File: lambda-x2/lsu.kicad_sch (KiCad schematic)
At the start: 56 parts, among them Q5 BSS169H6327, Q6 BSS169H6327, Q7 BSS169H6327, Q8 BSS169H6327, U12 MCP6002T-I/SN, U3 MCP6002T-I/SN, U9 GS8332-SR

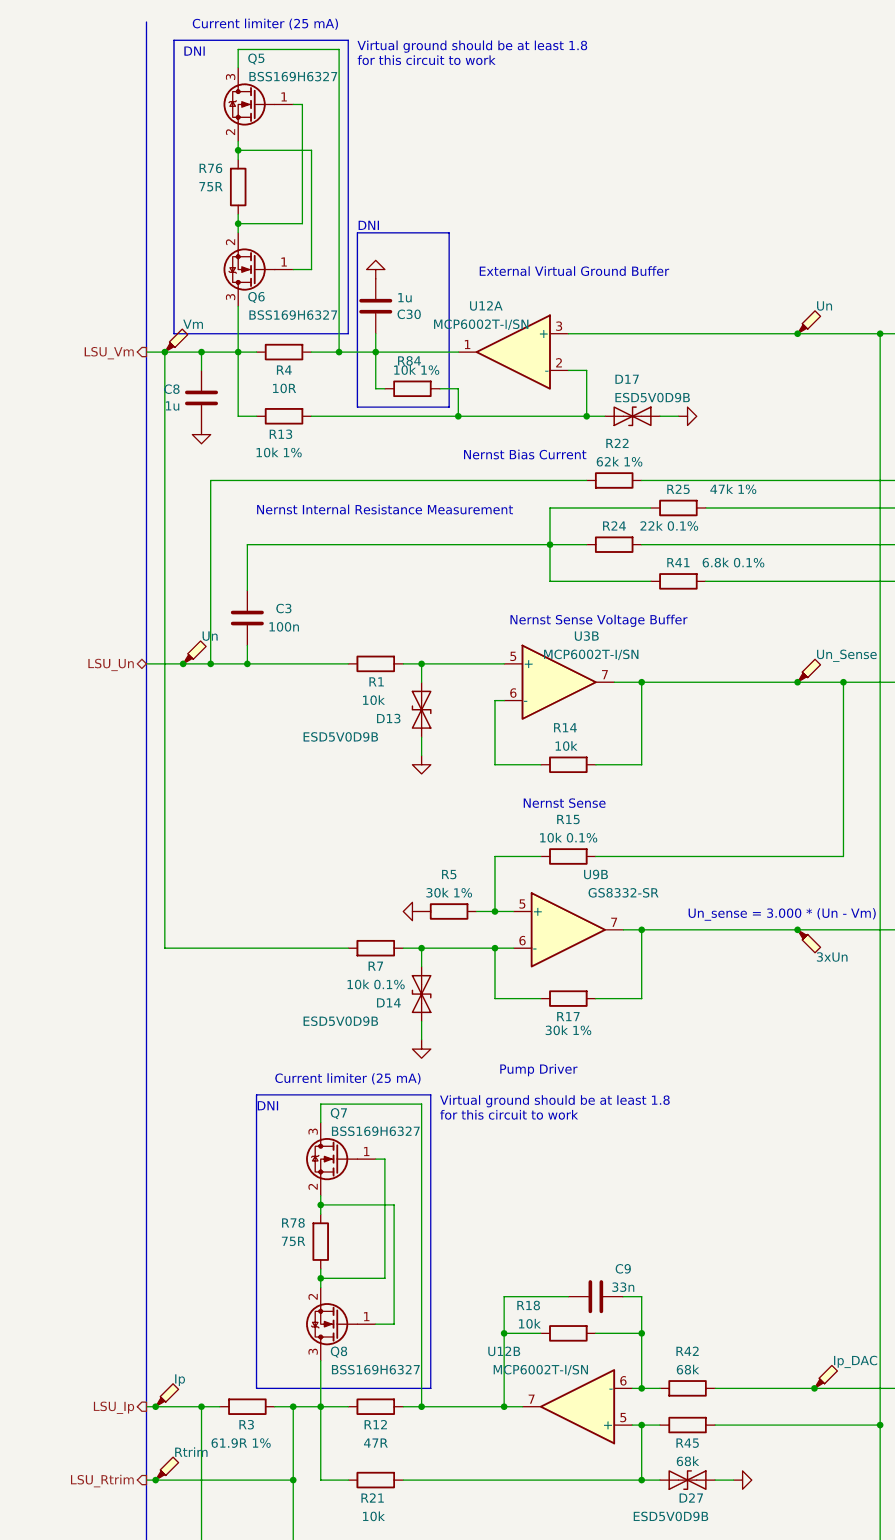
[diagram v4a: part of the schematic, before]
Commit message: lambda-x2: revork aux outputs, remove useless protection in LSU
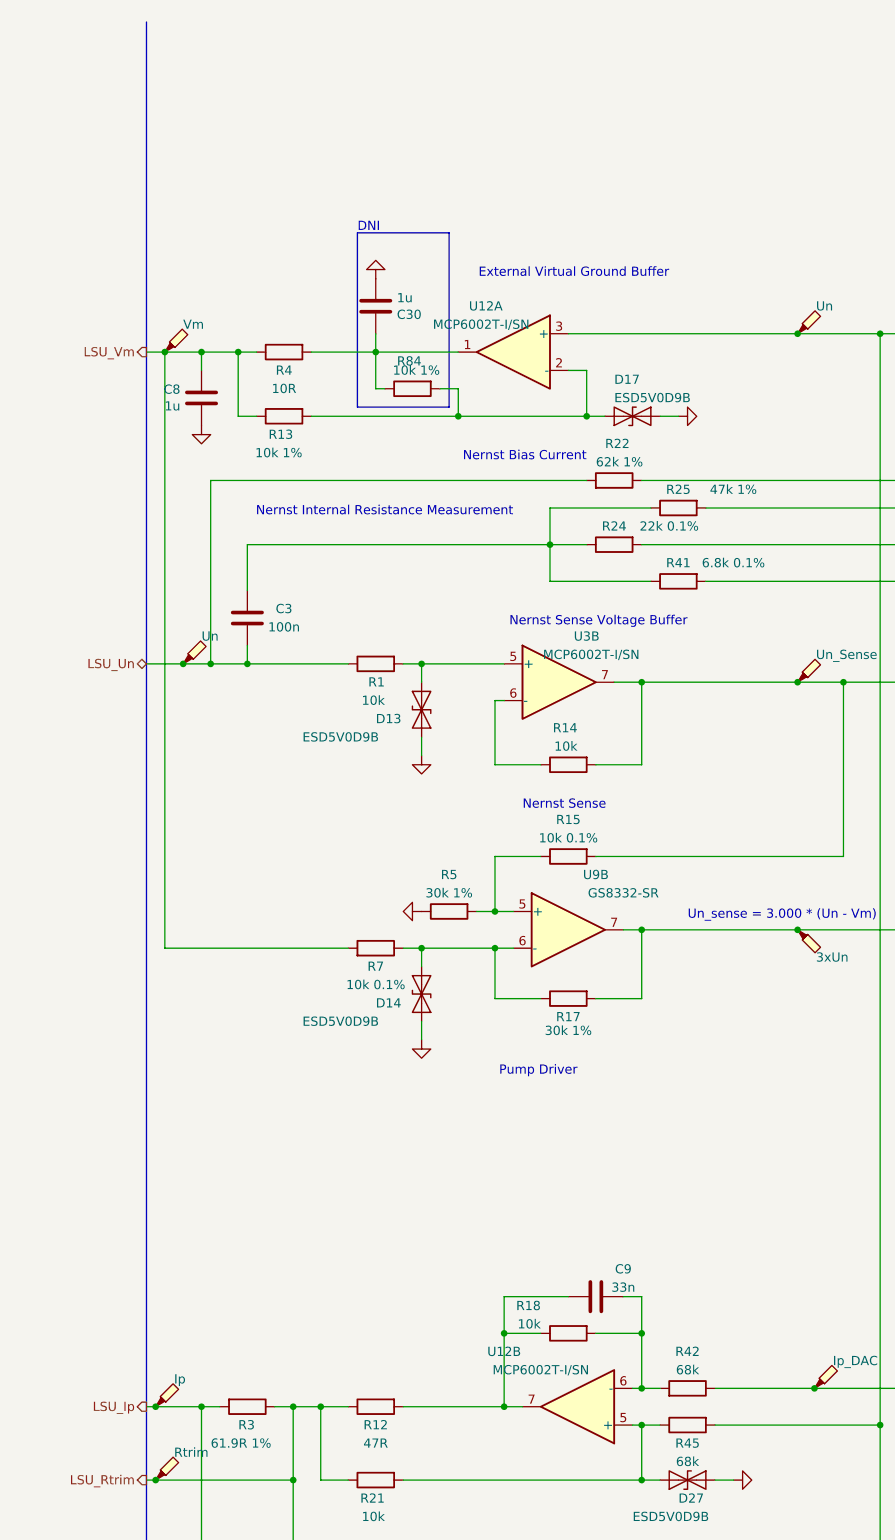
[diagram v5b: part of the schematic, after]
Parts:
- removed Q5, Q6, Q7, Q8: BSS169H6327, Package_TO_SOT_SMD:SOT-23, symbol Transistor_FET:BSS123
- removed R76, R78: 75R, Resistor_SMD:R_0603_1608Metric, symbol Device:R
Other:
- note removed: "Current limiter (25 mA)"
- note removed: "Virtual ground should be at least 1.8 for this circuit to work"

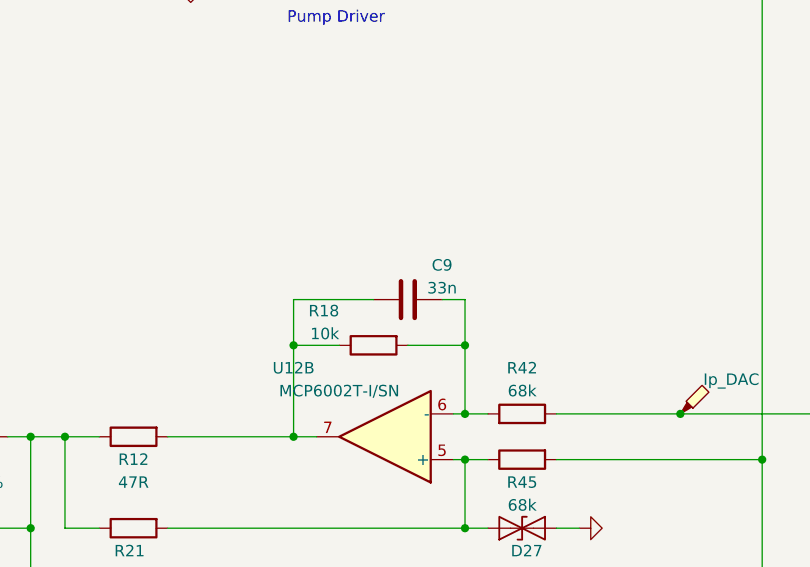
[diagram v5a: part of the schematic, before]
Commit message: lambda-x2: diagnostic for AUX out, PWM noise cancelation, etc
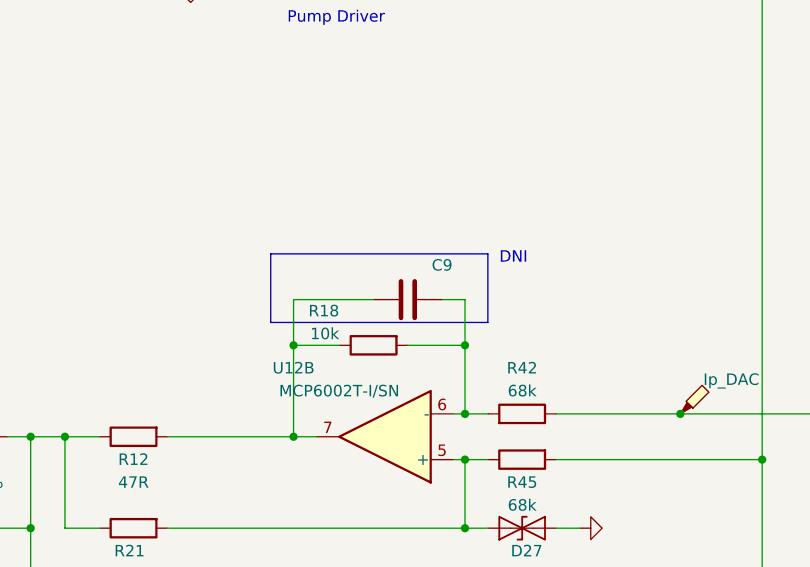
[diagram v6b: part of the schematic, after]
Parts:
- C9: value 33n -> (none); footprint Capacitor_SMD:C_0402_1005Metric -> (none); now left out of the parts list
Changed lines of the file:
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@@
+    (stroke (width 0) (type default) (color 0 0 0 0))
+  )
+  (polyline (pts (xy 151.13 204.47) (xy 151.13 196.85))
     (stroke (width 0) (type default) (color 0 0 0 0))
   )
@@
     (stroke (width 0) (type default) (color 0 0 0 0))
   )
+  (polyline (pts (xy 127 204.47) (xy 151.13 204.47))
+    (stroke (width 0) (type default) (color 0 0 0 0))
+  )
   (wire (pts (xy 227.33 167.64) (xy 227.33 162.56))
     (stroke (width 0) (type default) (color 0 0 0 0))
@@
     (stroke (width 0) (type default) (color 0 0 0 0))
   )
+  (polyline (pts (xy 127 196.85) (xy 127 204.47))
+    (stroke (width 0) (type default) (color 0 0 0 0))
+  )
   (wire (pts (xy 135.89 243.84) (xy 130.81 243.84))
     (stroke (width 0) (type default) (color 0 0 0 0))
@@
   )
   (wire (pts (xy 115.57 256.54) (xy 118.11 256.54))
+    (stroke (width 0) (type default) (color 0 0 0 0))
+  )
+  (polyline (pts (xy 151.13 196.85) (xy 127 196.85))
     (stroke (width 0) (type default) (color 0 0 0 0))
   )
@@
   (text "Nernst Internal Resistance Measurement" (at 130.81 93.98 180)
     (effects (font (size 1.27 1.27)) (justify right bottom))
+  )
+  (text "DNI" (at 152.4 198.12 0)
+    (effects (font (size 1.27 1.27)) (justify left bottom))
   )
   (text "caps for precision opamp" (at 210.82 237.49 0)
@@
   )
   (symbol (lib_id "Device:C") (at 142.24 201.93 90) (mirror x) (unit 1)
-    (in_bom yes) (on_board yes)
+    (in_bom no) (on_board yes)
     (property "Reference" "C9" (id 0) (at 146.05 198.12 90))
-    (property "Value" "33n" (id 1) (at 146.05 200.66 90))
-    (property "Footprint" "Capacitor_SMD:C_0402_1005Metric" (id 2) (at 146.05 202.8952 0)
-      (effects (font (size 1.27 1.27)) hide)
-    )
+    (property "Value" "" (id 1) (at 146.05 200.66 90))
+    (property "Footprint" "" (id 2) (at 146.05 202.8952 0)
+      (effects (font (size 1.27 1.27)) hide)
+    )

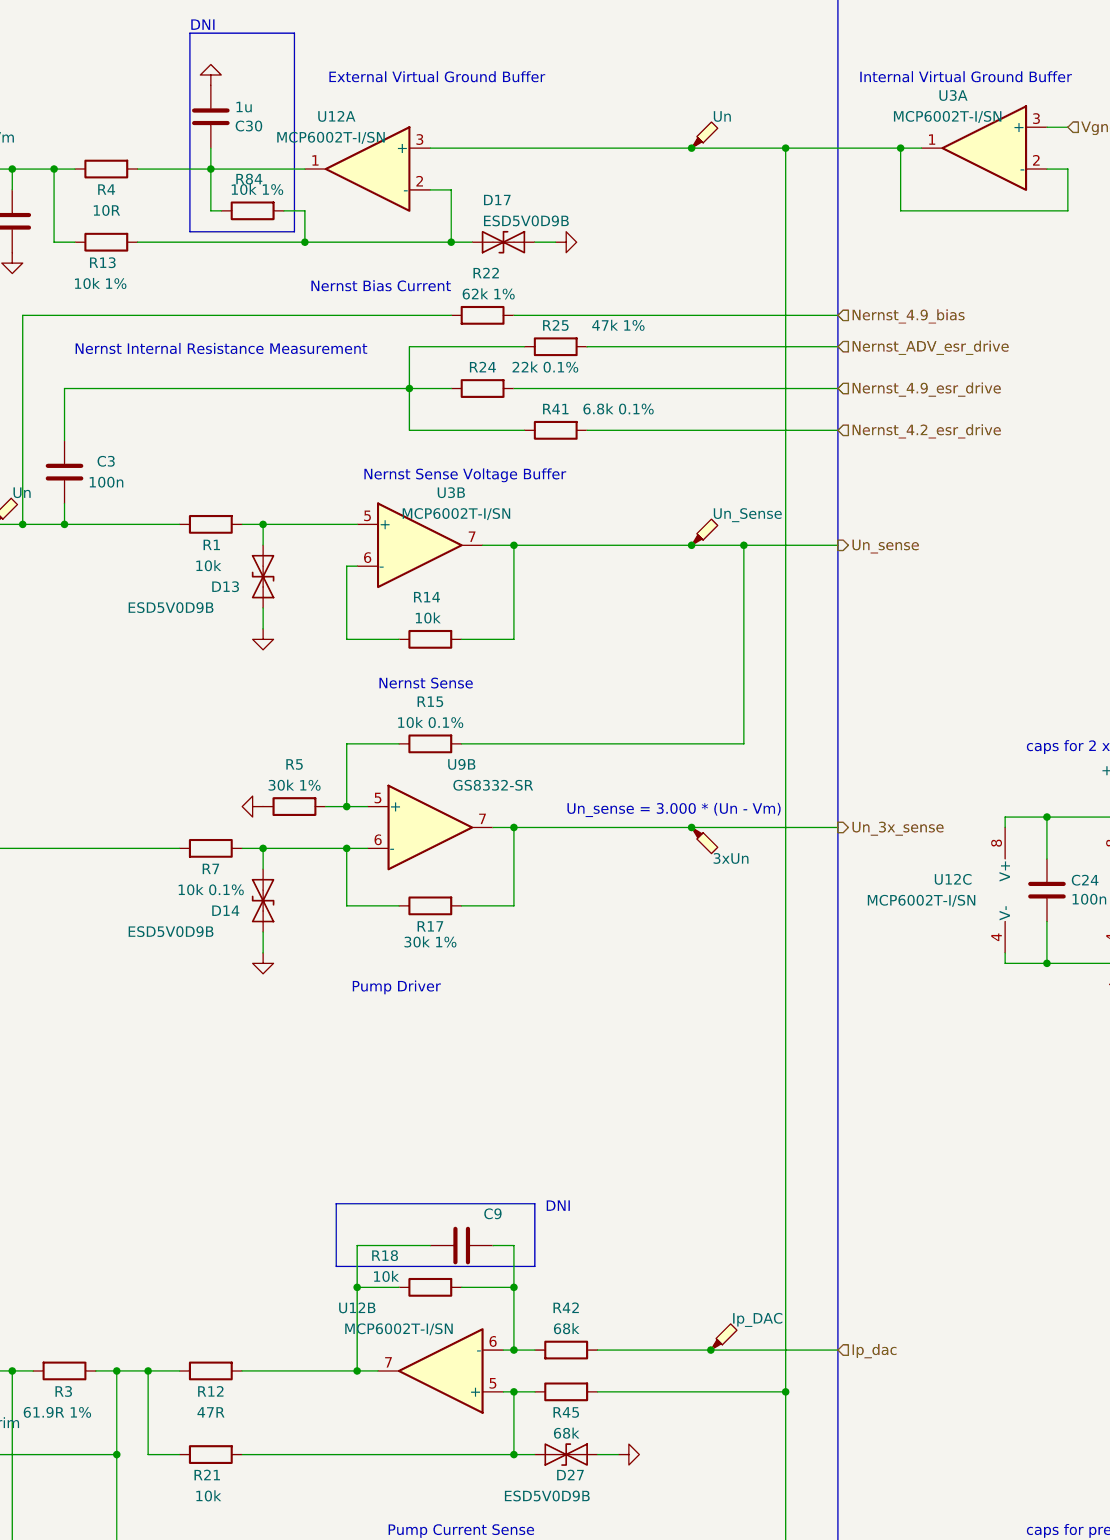
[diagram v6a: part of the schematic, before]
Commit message: lambda-x2: jtag, adc channels, one more led, BT en, etc
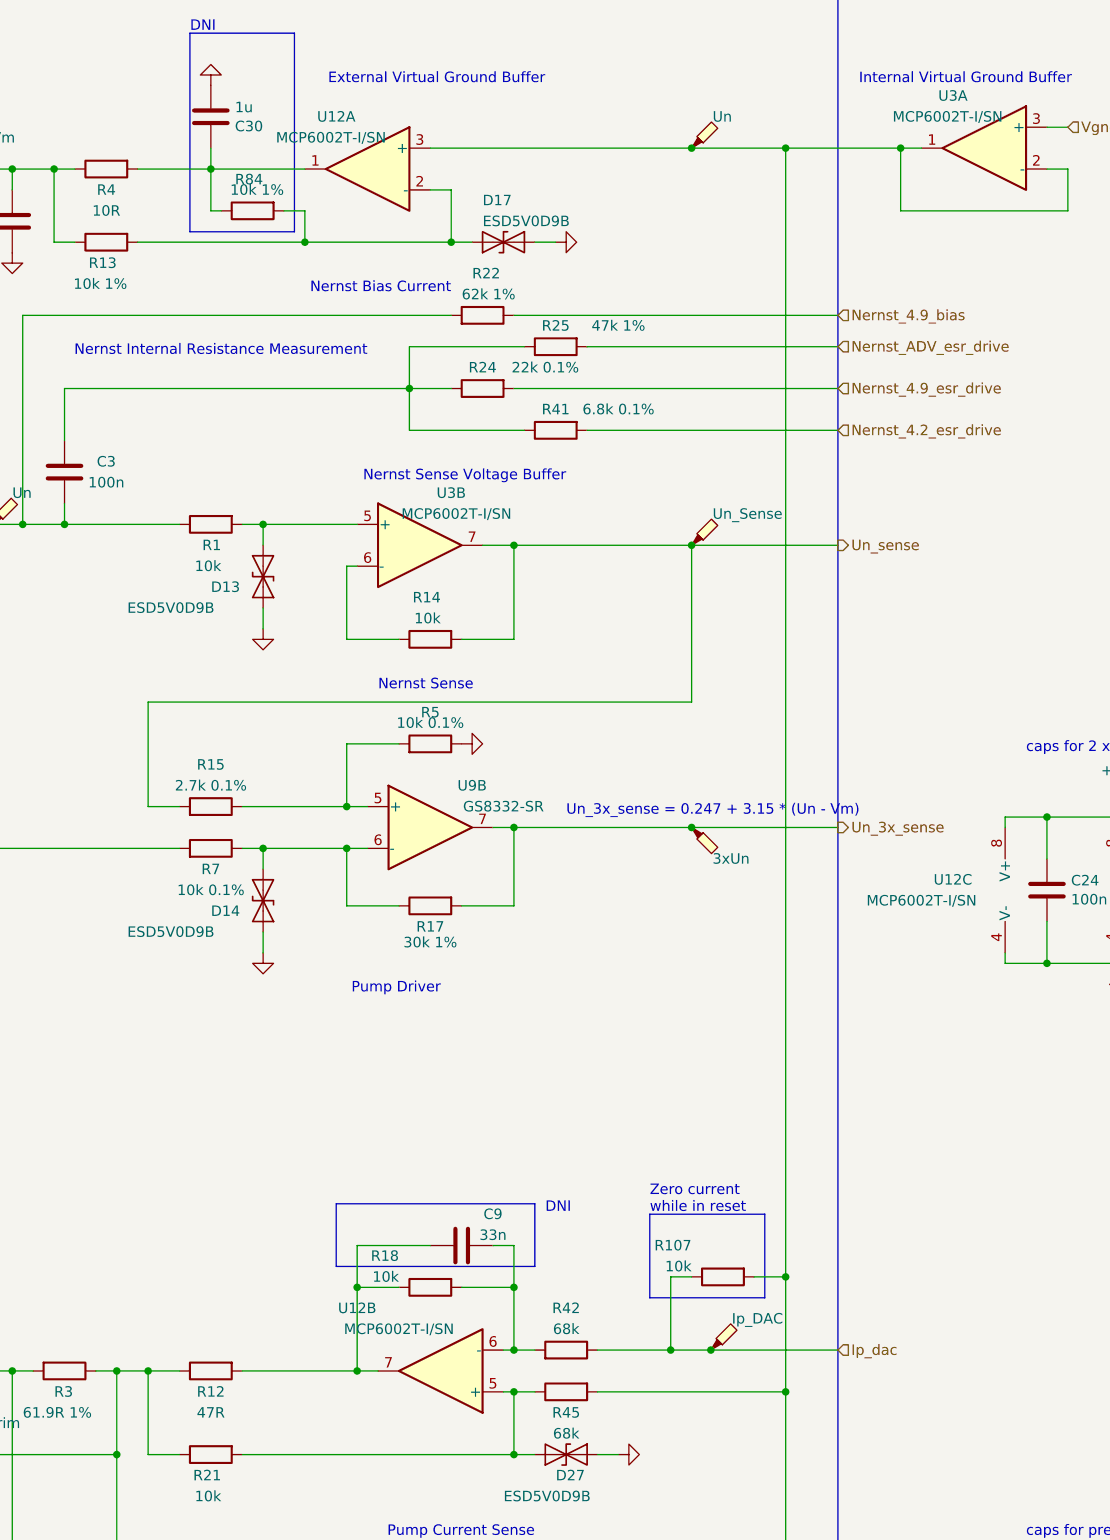
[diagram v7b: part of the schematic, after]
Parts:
- added R107: 10k, Resistor_SMD:R_0402_1005Metric, symbol Device:R
- C9: value (none) -> 33n; footprint (none) -> Capacitor_SMD:C_0402_1005Metric
- R15: value 10k 0.1% -> 2.7k 0.1%; LCSC C309083 -> C318131
- R5: value 30k 1% -> 10k 0.1%; LCSC C22984 -> C309083
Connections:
- net Ip_dac: now also R107.1
- net at R20.2, R45.2, TP14.1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: now also R107.2
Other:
- note added: "Un_3x_sense = 0.247 + 3.15 * (Un - Vm)"
- note added: "Zero current while in reset"
- note removed: "Un_sense = 3.000 * (Un - Vm)"
- moved on the sheet: R15, R5

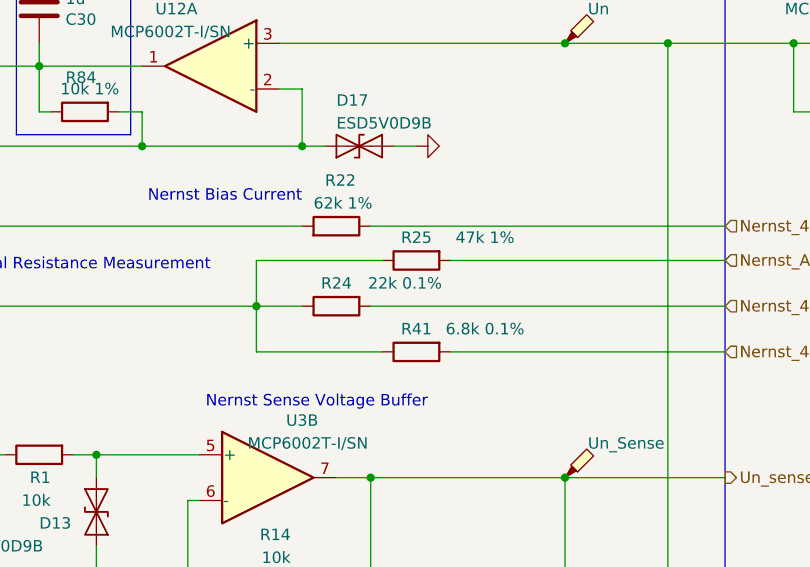
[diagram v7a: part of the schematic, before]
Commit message: lambda-x2: update BOM per JLC availability
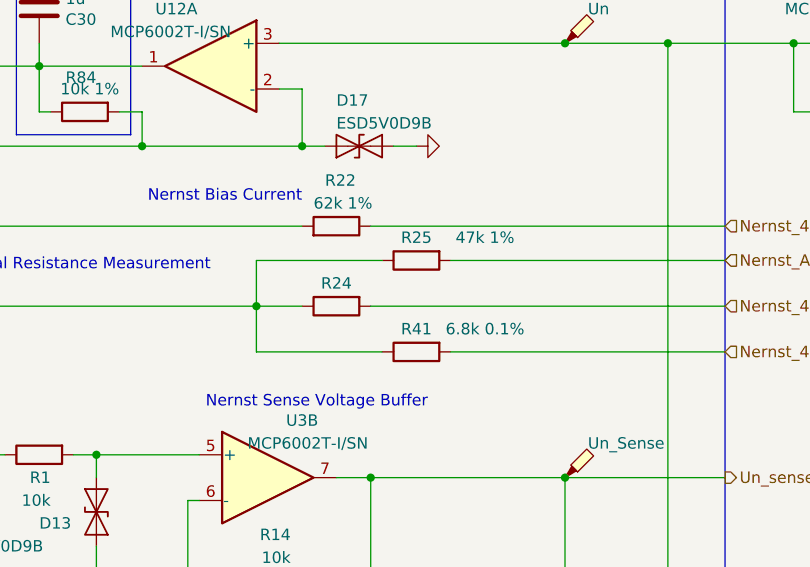
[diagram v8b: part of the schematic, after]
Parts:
- R24: value 22k 0.1% -> (none); footprint Resistor_SMD:R_0603_1608Metric -> (none); LCSC C133163 -> C705830
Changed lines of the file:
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@@
     (in_bom yes) (on_board yes)
     (property "Reference" "R24" (id 0) (at 144.78 95.25 90))
-    (property "Value" "22k 0.1%" (id 1) (at 152.4 95.25 90))
-    (property "Footprint" "Resistor_SMD:R_0603_1608Metric" (id 2) (at 144.78 96.012 90)
+    (property "Value" "" (id 1) (at 152.4 95.25 90))
+    (property "Footprint" "" (id 2) (at 144.78 96.012 90)
       (effects (font (size 1.27 1.27)) hide)
     )
@@
       (effects (font (size 1.27 1.27)) hide)
     )
-    (property "LCSC" "C133163" (id 4) (at 144.78 97.79 0)
+    (property "LCSC" "C705830" (id 4) (at 144.78 97.79 0)
       (effects (font (size 1.27 1.27)) hide)
     )
